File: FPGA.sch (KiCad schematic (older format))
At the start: 18 parts, among them U29 DSC6101CI2A-025.0000T, U30 10CL025YU256C8G

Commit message: PVT
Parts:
- removed R84: 0, Resistor-Chip:R_CHIP_1005_Hand_NoSilk, symbol passive:R
- renumbered C105 to C100, R81 to R72, R82 to R73, R83 to R74, R85 to R75, R86 to R76, RA9 to RA10, RA1 to RA2, RA2 to RA3, RA3 to RA4, RA4 to RA5, RA5 to RA6, RA6 to RA7, RA7 to RA8, RA8 to RA9, U29 to U27, U30 to U28
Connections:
- net FPGA_I2S_SCLK is gone; now on net +1V8: U28.M1 (CLK3/DIFFCLK_1n)
- net +1V8: no longer U28.H12 (MSEL1)
- net GND: now also U28.E2 (CLK0/DIFFCLK_0p)
- net TDO: now also U28.J4 (TDO)
- net FPGA_I2S_DIN: no longer names the net of U28.K2 (IO/L10p)
- net FPGA_I2S_DOUT: no longer names the net of U28.L1 (IO/L11n)
- net FPGA_I2S_FS: no longer names the net of U28.L2 (IO/DPCLK1/L11p)
- net ~GP_FAULT renamed ~FPGA_STOP
- new net +2V5: U28.H12 (MSEL1)

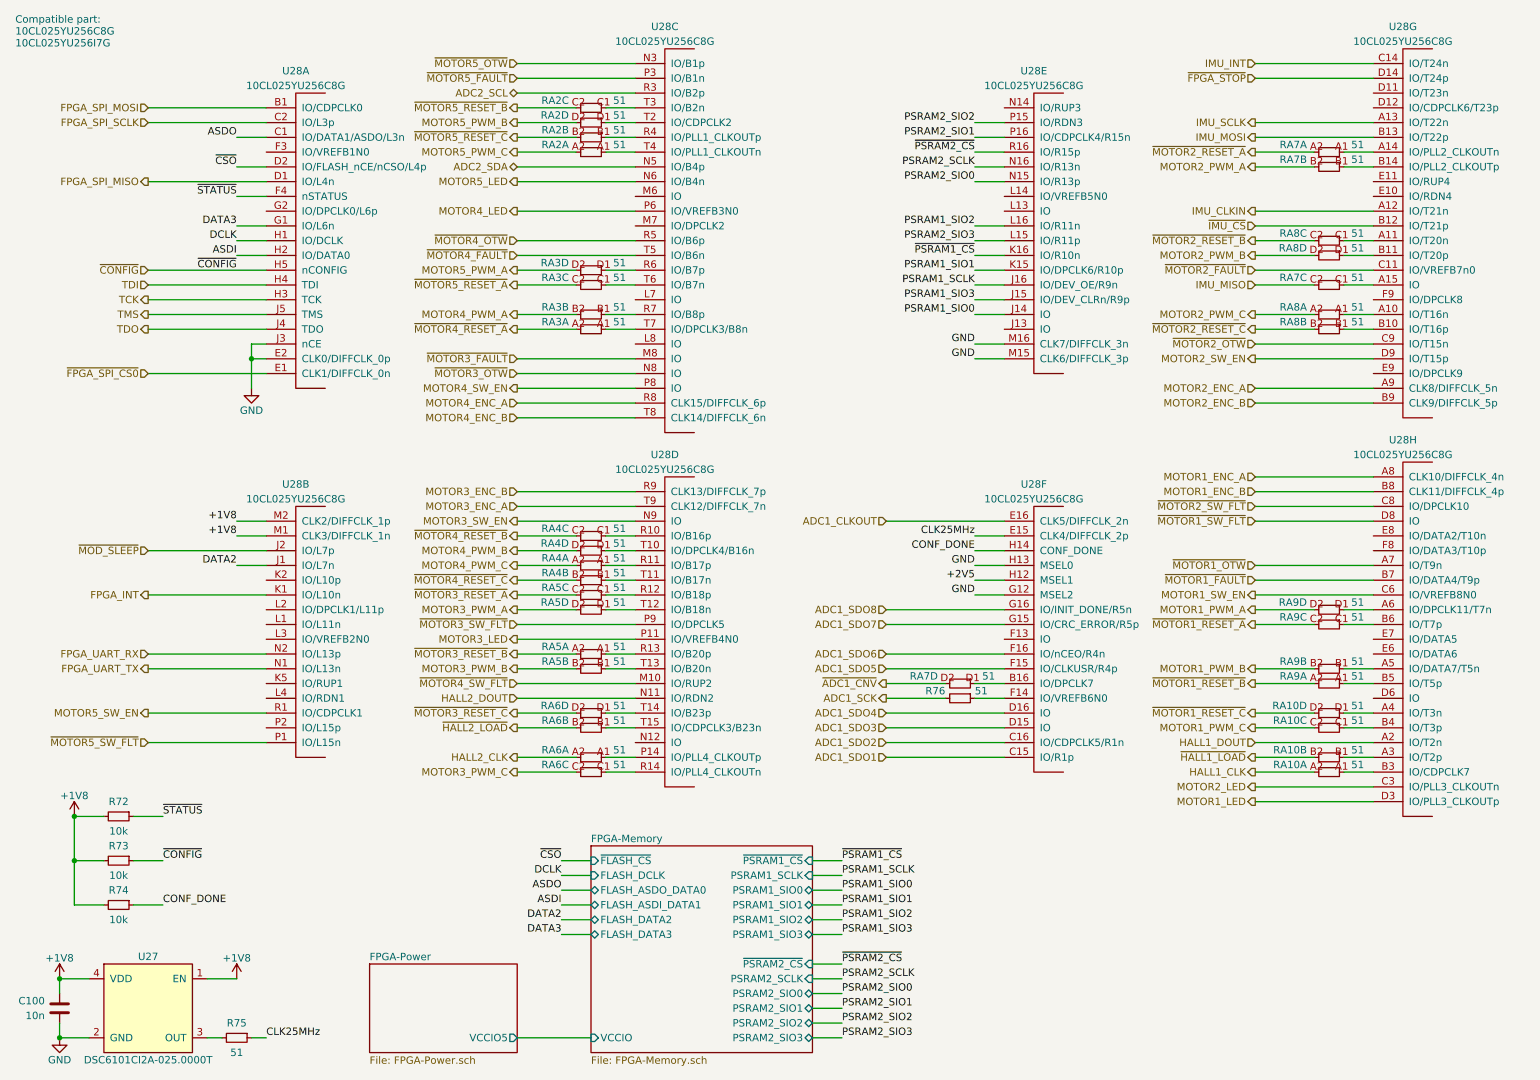
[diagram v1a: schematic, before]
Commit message: SBUにTVSダイオードを追加
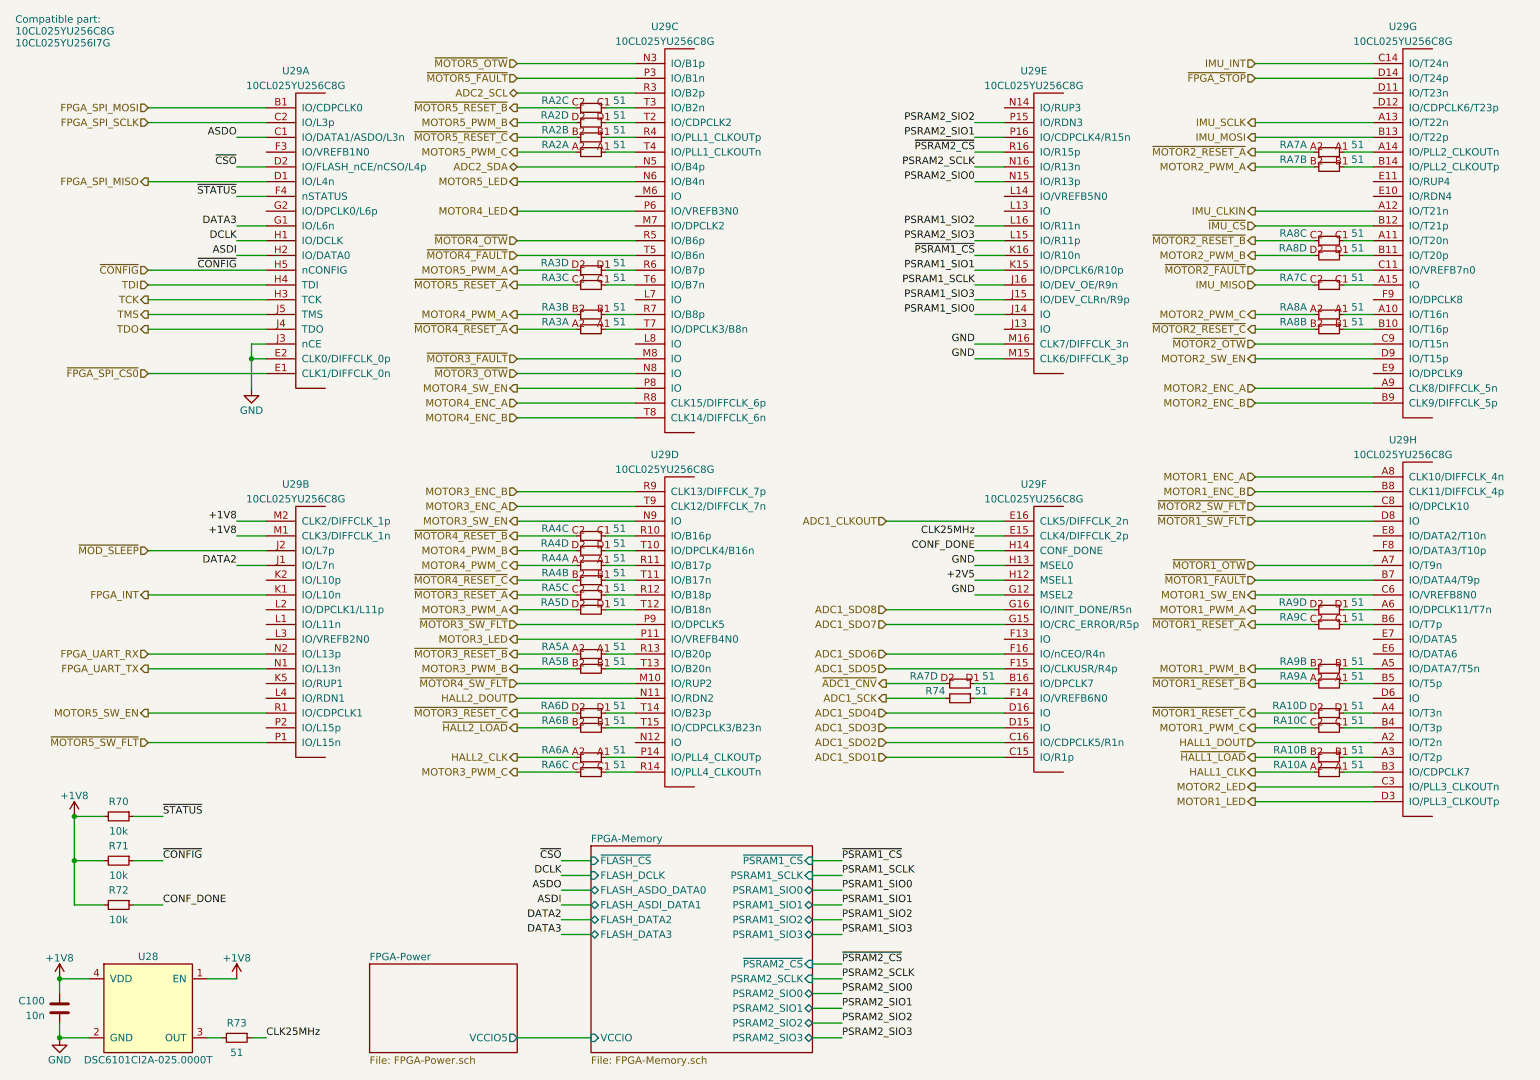
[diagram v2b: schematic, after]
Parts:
- renumbered R72 to R70, R73 to R71, R74 to R72, R75 to R73, R76 to R74, U27 to U28, U28 to U29
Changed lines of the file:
@@
 P 2500 2100
 AR Path="/5E41CBB4" Ref="U?"  Part="1"
-AR Path="/5E4B5786/5E41CBB4" Ref="U28"  Part="1"
-F 0 "U28" H 2500 3250 50  0000 C CNN
+AR Path="/5E4B5786/5E41CBB4" Ref="U29"  Part="1"
+F 0 "U29" H 2500 3250 50  0000 C CNN
 F 1 "10CL025YU256C8G" H 2500 3150 50  0000 C CNN
 F 2 "Phoenix:BGA256_14.0x14.0_P0.8" H 2500 2100 50  0001 C CNN
@@
 P 2500 4800
 AR Path="/5E423EC1" Ref="U?"  Part="2"
-AR Path="/5E4B5786/5E423EC1" Ref="U28"  Part="2"
-F 0 "U28" H 2500 5850 50  0000 C CNN
+AR Path="/5E4B5786/5E423EC1" Ref="U29"  Part="2"
+F 0 "U29" H 2500 5850 50  0000 C CNN
 F 1 "10CL025YU256C8G" H 2500 5750 50  0000 C CNN
 F 2 "Phoenix:BGA256_14.0x14.0_P0.8" H 2500 4800 50  0001 C CNN
@@
 P 5000 2100
 AR Path="/5E426E27" Ref="U?"  Part="3"
-AR Path="/5E4B5786/5E426E27" Ref="U28"  Part="3"
-F 0 "U28" H 5000 3550 50  0000 C CNN
+AR Path="/5E4B5786/5E426E27" Ref="U29"  Part="3"
+F 0 "U29" H 5000 3550 50  0000 C CNN
 F 1 "10CL025YU256C8G" H 5000 3450 50  0000 C CNN
 F 2 "Phoenix:BGA256_14.0x14.0_P0.8" H 5000 2100 50  0001 C CNN
@@
 P 5000 4800
 AR Path="/5E428304" Ref="U?"  Part="4"
-AR Path="/5E4B5786/5E428304" Ref="U28"  Part="4"
-F 0 "U28" H 5000 6050 50  0000 C CNN
+AR Path="/5E4B5786/5E428304" Ref="U29"  Part="4"
+F 0 "U29" H 5000 6050 50  0000 C CNN
 F 1 "10CL025YU256C8G" H 5000 5950 50  0000 C CNN
 F 2 "Phoenix:BGA256_14.0x14.0_P0.8" H 5000 4800 50  0001 C CNN
@@
 P 7500 2100
 AR Path="/5E42B7FD" Ref="U?"  Part="5"
-AR Path="/5E4B5786/5E42B7FD" Ref="U28"  Part="5"
-F 0 "U28" H 7500 3250 50  0000 C CNN
+AR Path="/5E4B5786/5E42B7FD" Ref="U29"  Part="5"
+F 0 "U29" H 7500 3250 50  0000 C CNN
 F 1 "10CL025YU256C8G" H 7500 3150 50  0000 C CNN
 F 2 "Phoenix:BGA256_14.0x14.0_P0.8" H 7500 2100 50  0001 C CNN
@@
 P 7500 4800
 AR Path="/5E42E6BB" Ref="U?"  Part="6"
-AR Path="/5E4B5786/5E42E6BB" Ref="U28"  Part="6"
-F 0 "U28" H 7500 5850 50  0000 C CNN
+AR Path="/5E4B5786/5E42E6BB" Ref="U29"  Part="6"
+F 0 "U29" H 7500 5850 50  0000 C CNN
 F 1 "10CL025YU256C8G" H 7500 5750 50  0000 C CNN
 F 2 "Phoenix:BGA256_14.0x14.0_P0.8" H 7500 4800 50  0001 C CNN
@@
 P 10000 2100
 AR Path="/5E430C91" Ref="U?"  Part="7"
-AR Path="/5E4B5786/5E430C91" Ref="U28"  Part="7"
-F 0 "U28" H 10000 3550 50  0000 C CNN
+AR Path="/5E4B5786/5E430C91" Ref="U29"  Part="7"
+F 0 "U29" H 10000 3550 50  0000 C CNN
 F 1 "10CL025YU256C8G" H 10000 3450 50  0000 C CNN
 F 2 "Phoenix:BGA256_14.0x14.0_P0.8" H 10000 2100 50  0001 C CNN
@@
 P 10000 4800
 AR Path="/5E43236C" Ref="U?"  Part="8"
-AR Path="/5E4B5786/5E43236C" Ref="U28"  Part="8"
-F 0 "U28" H 10000 6150 50  0000 C CNN
+AR Path="/5E4B5786/5E43236C" Ref="U29"  Part="8"
+F 0 "U29" H 10000 6150 50  0000 C CNN
 F 1 "10CL025YU256C8G" H 10000 6050 50  0000 C CNN
 F 2 "Phoenix:BGA256_14.0x14.0_P0.8" H 10000 4800 50  0001 C CNN
@@
 	2300 3000 1500 3000
 $Comp
-L oscillator:Oscillator_(EN)(GND)(OUT)(VDD) U27
+L oscillator:Oscillator_(EN)(GND)(OUT)(VDD) U28
 U 1 1 5EF189B5
 P 1500 7300
-F 0 "U27" H 1500 7650 50  0000 C CNN
+F 0 "U28" H 1500 7650 50  0000 C CNN
 F 1 "DSC6101CI2A-025.0000T" H 1500 6950 50  0000 C CNN
 F 2 "Oscillator-Generic:DSC6xxxC" H 1500 7300 50  0001 C CNN
@@
 Connection ~ 900  7500
 $Comp
-L passive:R R75
+L passive:R R73
 U 1 1 5EF87876
 P 2100 7500
-F 0 "R75" V 2000 7500 50  0000 C CNN
+F 0 "R73" V 2000 7500 50  0000 C CNN
 F 1 "51" V 2200 7500 50  0000 C CNN
 F 2 "Resistor-Chip:R_CHIP_1005_Hand_NoSilk" V 2150 7400 50  0001 C CNN
@@
 CLK25MHz
 $Comp
-L passive:R R76
+L passive:R R74
 U 1 1 5ED7970F
 P 7000 5200
-F 0 "R76" V 6950 5100 50  0000 R CNN
+F 0 "R74" V 6950 5100 50  0000 R CNN
 F 1 "51" V 6950 5300 50  0000 L CNN
 F 2 "Resistor-Chip:R_CHIP_1005_Hand_NoSilk" V 7050 5100 50  0001 C CNN
@@
 ~CONFIG
 $Comp
-L passive:R R73
+L passive:R R71
 U 1 1 5FF76326
 P 1300 6300
-F 0 "R73" V 1200 6300 50  0000 C CNN
+F 0 "R71" V 1200 6300 50  0000 C CNN
 F 1 "10k" V 1400 6300 50  0000 C CNN
 F 2 "Resistor-Chip:R_CHIP_1005_Hand_NoSilk" V 1350 6200 50  0001 C CNN
@@
 	1400 6300 1600 6300
 $Comp
-L passive:R R72
+L passive:R R70
 U 1 1 5FFA8123
 P 1300 6000
-F 0 "R72" V 1200 6000 50  0000 C CNN
+F 0 "R70" V 1200 6000 50  0000 C CNN
 F 1 "10k" V 1400 6000 50  0000 C CNN
 F 2 "Resistor-Chip:R_CHIP_1005_Hand_NoSilk" V 1350 5900 50  0001 C CNN
@@
 $EndComp
 $Comp
-L passive:R R74
+L passive:R R72
 U 1 1 5FFA8457
 P 1300 6600
-F 0 "R74" V 1200 6600 50  0000 C CNN
+F 0 "R72" V 1200 6600 50  0000 C CNN
 F 1 "10k" V 1400 6600 50  0000 C CNN
 F 2 "Resistor-Chip:R_CHIP_1005_Hand_NoSilk" V 1350 6500 50  0001 C CNN

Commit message: FPGA_INTをFPGA_MODEに変更
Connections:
- net FPGA_INT renamed FPGA_MODE
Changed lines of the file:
@@
 Text HLabel 1500 1700 0    50   Output ~ 0
 FPGA_SPI_MISO
-Text HLabel 1500 4500 0    50   Output ~ 0
-FPGA_INT
+Text HLabel 1500 4500 0    50   Input ~ 0
+FPGA_MODE
 Wire Wire Line
 	1500 2400 2300 2400
